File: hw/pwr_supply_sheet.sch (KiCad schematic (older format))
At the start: 17 parts

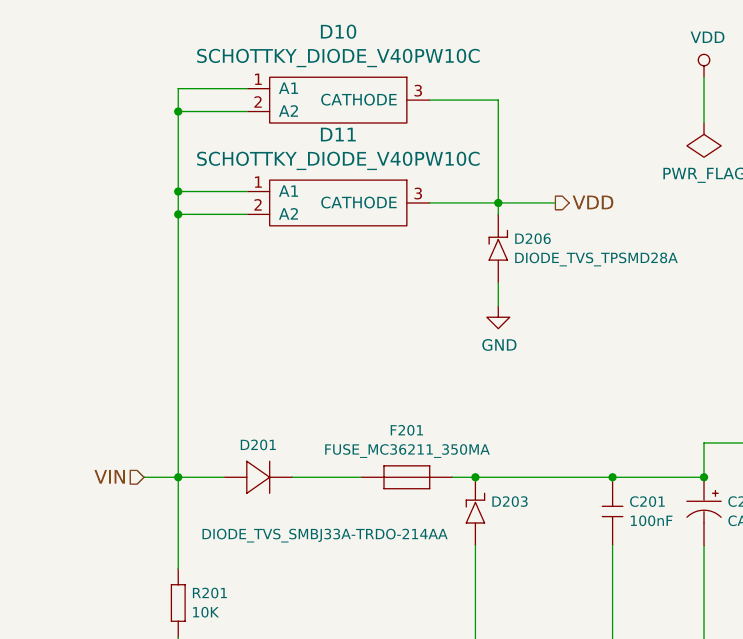
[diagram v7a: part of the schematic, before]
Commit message: reverse protection diodes removed
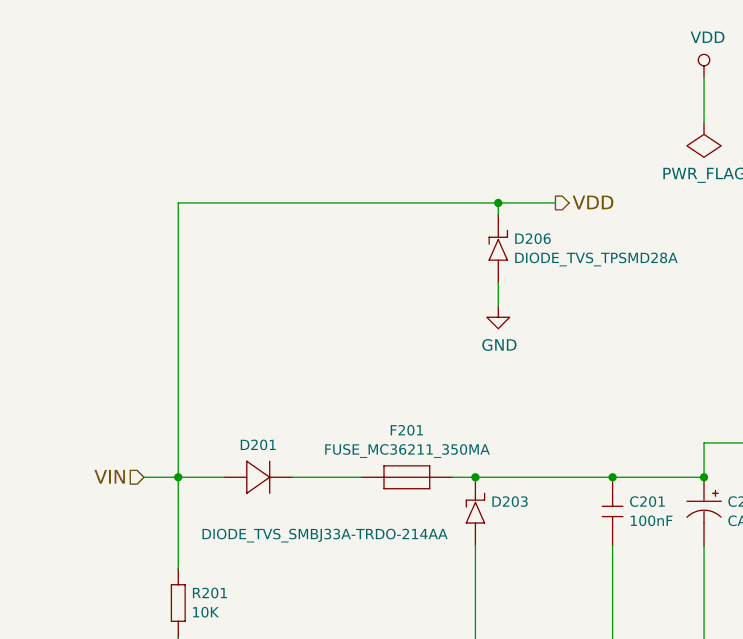
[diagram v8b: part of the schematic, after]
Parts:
- removed D10, D11: SCHOTTKY_DIODE_V40PW10C, usevolt:SlimDPAK, symbol usevolt:SCHOTTKY_DIODE_V40PW10C
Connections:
- net VIN is gone; now on net VDD: D201.P$1 (P), R201.2 (R2)
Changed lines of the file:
@@
 Wire Wire Line
 	2900 2650 3150 2650
-$Comp
-L usevolt:SCHOTTKY_DIODE_V40PW10C D10
-U 1 1 5C521B18
-P 2200 2250
-F 0 "D10" H 2200 2597 60  0000 C CNN
-F 1 "SCHOTTKY_DIODE_V40PW10C" H 2200 2491 60  0000 C CNN
-F 2 "usevolt:SlimDPAK" H 2000 1900 60  0001 C CNN
-F 3 "http://www.farnell.com/datasheets/2245239.pdf?_ga=2.16591231.874534928.1505194133-1862443086.1504075057" H 2000 1900 60  0001 C CNN
-F 4 "2535169" H 2550 2850 60  0001 C CNN "1st Source Part Number"
-F 5 "Digikey" H 2650 2950 60  0001 C CNN "2nd Source"
-F 6 "Farnell" H 2450 2750 60  0001 C CNN "1st Source"
-F 7 "V40PW10CHM3/I" H 2350 2650 60  0001 C CNN "Manufacturer Part Number"
-F 8 "V40PW10CHM3/IGICT-ND" H 2750 3050 60  0001 C CNN "2nd Source Part Number"
-F 9 "VISHAY" H 2250 2550 60  0001 C CNN "Manufacturer"
-	1    2200 2250
-	1    0    0    -1
-$EndComp
-$Comp
-L usevolt:SCHOTTKY_DIODE_V40PW10C D11
-U 1 1 5C5227A8
-P 2200 2700
-F 0 "D11" H 2200 3047 60  0000 C CNN
-F 1 "SCHOTTKY_DIODE_V40PW10C" H 2200 2941 60  0000 C CNN
-F 2 "usevolt:SlimDPAK" H 2000 2350 60  0001 C CNN
-F 3 "http://www.farnell.com/datasheets/2245239.pdf?_ga=2.16591231.874534928.1505194133-1862443086.1504075057" H 2000 2350 60  0001 C CNN
-F 4 "2535169" H 2550 3300 60  0001 C CNN "1st Source Part Number"
-F 5 "Digikey" H 2650 3400 60  0001 C CNN "2nd Source"
-F 6 "Farnell" H 2450 3200 60  0001 C CNN "1st Source"
-F 7 "V40PW10CHM3/I" H 2350 3100 60  0001 C CNN "Manufacturer Part Number"
-F 8 "V40PW10CHM3/IGICT-ND" H 2750 3500 60  0001 C CNN "2nd Source Part Number"
-F 9 "VISHAY" H 2250 3000 60  0001 C CNN "Manufacturer"
-	1    2200 2700
-	1    0    0    -1
-$EndComp
-Wire Wire Line
-	1500 2150 1800 2150
-Wire Wire Line
-	1500 2150 1500 2250
-Wire Wire Line
-	1800 2250 1500 2250
-Connection ~ 1500 2250
-Wire Wire Line
-	1500 2250 1500 2600
-Wire Wire Line
-	1800 2600 1500 2600
-Connection ~ 1500 2600
-Wire Wire Line
-	1500 2600 1500 2700
-Wire Wire Line
-	1800 2700 1500 2700
-Connection ~ 1500 2700
-Wire Wire Line
-	1500 2700 1500 3850
-Wire Wire Line
-	2600 2650 2900 2650
 Connection ~ 2900 2650
-Wire Wire Line
-	2900 2650 2900 2200
-Wire Wire Line
-	2900 2200 2600 2200
 $Comp
 L kemet:100nF C1
@@
 	-1   0    0    1
 $EndComp
+Wire Wire Line
+	1500 2650 2900 2650
+Wire Wire Line
+	1500 2650 1500 3850
 $EndSCHEMATC
